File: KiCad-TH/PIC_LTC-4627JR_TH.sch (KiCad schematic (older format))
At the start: 17 parts, among them J1 Conn_01x05_Male, J2 Conn_01x04, Q1 Q_NPN_EBC, Q2 Q_NPN_EBC, Q3 Q_NPN_EBC, Q4 Q_NPN_EBC, Q5 Q_NPN_EBC, U1 PIC16F18344-P

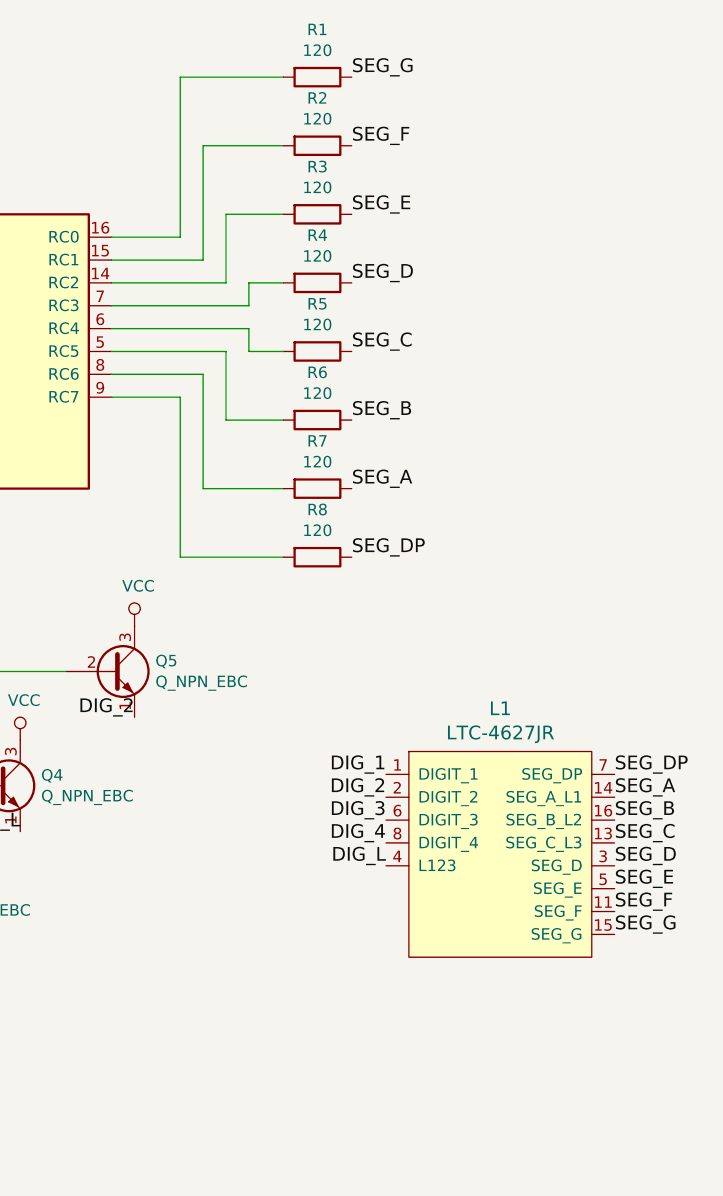
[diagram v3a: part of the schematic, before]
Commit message: Direct connect pins for segments from PIC to LED
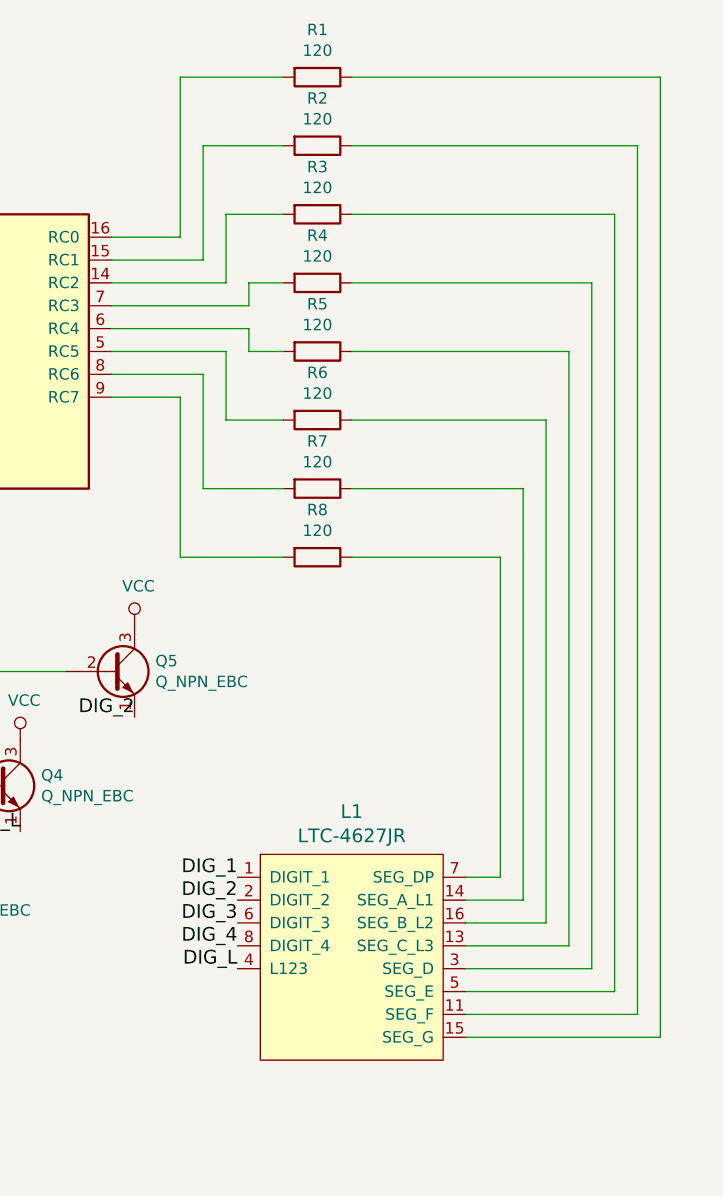
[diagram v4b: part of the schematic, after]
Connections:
- net SEG_A: no longer names the net of L1.14 (SEG_A_L1), R7.1
- net SEG_B: no longer names the net of L1.16 (SEG_B_L2), R6.1
- net SEG_C: no longer names the net of L1.13 (SEG_C_L3), R5.1
- net SEG_D: no longer names the net of L1.3 (SEG_D), R4.1
- net SEG_DP: no longer names the net of L1.7 (SEG_DP), R8.1
- net SEG_E: no longer names the net of L1.5 (SEG_E), R3.1
- net SEG_F: no longer names the net of L1.11 (SEG_F), R2.1
- net SEG_G: no longer names the net of L1.15 (SEG_G), R1.1
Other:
- moved on the sheet: L1
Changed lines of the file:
@@
 Wire Wire Line
 	5300 4200 5750 4200
-Text Label 6050 2100 0    60   ~ 0
-SEG_G
-Text Label 6050 2400 0    60   ~ 0
-SEG_F
-Text Label 6050 2700 0    60   ~ 0
-SEG_E
-Text Label 6050 3000 0    60   ~ 0
-SEG_D
-Text Label 6050 3300 0    60   ~ 0
-SEG_C
-Text Label 6050 3600 0    60   ~ 0
-SEG_B
-Text Label 6050 3900 0    60   ~ 0
-SEG_A
-Text Label 6050 4200 0    60   ~ 0
-SEG_DP
 $Comp
 L VCC #PWR013
@@
 L LTC-4627JR L1
 U 1 1 59CC84A7
-P 6700 4950
-F 0 "L1" H 6700 5037 60  0000 C CNN
-F 1 "LTC-4627JR" H 6700 4931 60  0000 C CNN
-F 2 "" H 6700 4950 60  0001 C CNN
-F 3 "" H 6700 4950 60  0001 C CNN
-	1    6700 4950
-	1    0    0    -1
-$EndComp
-Text Label 6200 5150 2    60   ~ 0
+P 6050 5400
+F 0 "L1" H 6050 5487 60  0000 C CNN
+F 1 "LTC-4627JR" H 6050 5381 60  0000 C CNN
+F 2 "" H 6050 5400 60  0001 C CNN
+F 3 "" H 6050 5400 60  0001 C CNN
+	1    6050 5400
+	1    0    0    -1
+$EndComp
+Text Label 5550 5600 2    60   ~ 0
 DIG_1
-Text Label 6200 5250 2    60   ~ 0
+Text Label 5550 5700 2    60   ~ 0
 DIG_2
-Text Label 6200 5350 2    60   ~ 0
+Text Label 5550 5800 2    60   ~ 0
 DIG_3
-Text Label 6200 5450 2    60   ~ 0
+Text Label 5550 5900 2    60   ~ 0
 DIG_4
-Text Label 6200 5550 2    60   ~ 0
+Text Label 5550 6000 2    60   ~ 0
 DIG_L
-Text Label 7200 5150 0    60   ~ 0
-SEG_DP
-Text Label 7200 5250 0    60   ~ 0
-SEG_A
-Text Label 7200 5350 0    60   ~ 0
-SEG_B
-Text Label 7200 5450 0    60   ~ 0
-SEG_C
-Text Label 7200 5550 0    60   ~ 0
-SEG_D
-Text Label 7200 5650 0    60   ~ 0
-SEG_E
-Text Label 7200 5750 0    60   ~ 0
-SEG_F
-Text Label 7200 5850 0    60   ~ 0
-SEG_G
 $Comp
 L PWR_FLAG #FLG01
@@
 	1    0    0    -1
 $EndComp
+Wire Wire Line
+	6550 5600 6700 5600
+Wire Wire Line
+	6700 5600 6700 4200
+Wire Wire Line
+	6700 4200 6050 4200
+Wire Wire Line
+	6550 5700 6800 5700
+Wire Wire Line
+	6800 5700 6800 3900
+Wire Wire Line
+	6800 3900 6050 3900
+Wire Wire Line
+	6550 5800 6900 5800
+Wire Wire Line
+	6900 5800 6900 3600
+Wire Wire Line
+	6900 3600 6050 3600
+Wire Wire Line
+	6550 5900 7000 5900
+Wire Wire Line
+	7000 5900 7000 3300
+Wire Wire Line
+	7000 3300 6050 3300
+Wire Wire Line
+	6550 6000 7100 6000
+Wire Wire Line
+	7100 6000 7100 3000
+Wire Wire Line
+	7100 3000 6050 3000
+Wire Wire Line
+	6550 6100 7200 6100
+Wire Wire Line
+	7200 6100 7200 2700
+Wire Wire Line
+	7200 2700 6050 2700
+Wire Wire Line
+	6550 6200 7300 6200
+Wire Wire Line
+	7300 6200 7300 2400
+Wire Wire Line
+	7300 2400 6050 2400
+Wire Wire Line
+	6550 6300 7400 6300
+Wire Wire Line
+	7400 6300 7400 2100
+Wire Wire Line
+	7400 2100 6050 2100
 $EndSCHEMATC
